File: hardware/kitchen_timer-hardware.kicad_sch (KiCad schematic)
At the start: 33 parts, among them J1 AVR-ISP-6, Q1 IRLML6402, SW1 SW_Push_Open_Dual, U1 ATmega328P-A, U2 BMS Module, U3 UART_Module, U4 AP2111H-3.3, U5 TPS61200DRC, Y1 Crystal

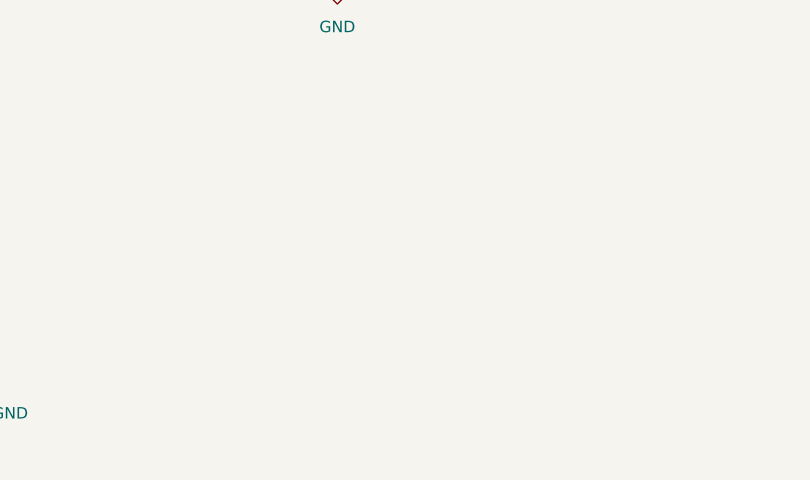
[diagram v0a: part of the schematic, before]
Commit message: Added the LED Matrices Driers as a hierarchical schematic.
I used the herachical schmatic feature cause it gives us more space to work on and organize connections.
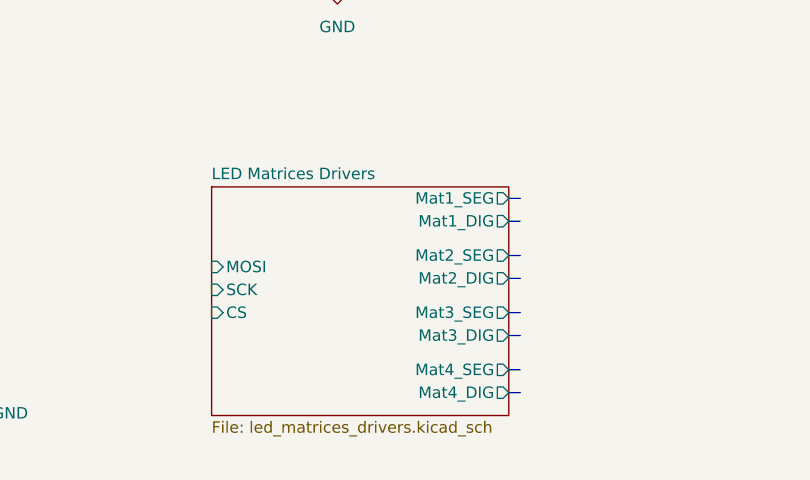
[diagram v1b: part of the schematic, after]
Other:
- added sheet LED Matrices Drivers (led_matrices_drivers.kicad_sch)
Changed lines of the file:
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@@
 		(at 109.22 30.48)
 	)
+	(bus
+		(pts
+			(xy 162.56 157.48) (xy 163.83 157.48)
+		)
+		(stroke
+			(width 0)
+			(type default)
+		)
+	)
 	(wire
 		(pts
@@
 		)
 	)
+	(bus
+		(pts
+			(xy 162.56 163.83) (xy 163.83 163.83)
+		)
+		(stroke
+			(width 0)
+			(type default)
+		)
+	)
 	(wire
 		(pts
@@
 		)
 	)
+	(bus
+		(pts
+			(xy 162.56 153.67) (xy 163.83 153.67)
+		)
+		(stroke
+			(width 0)
+			(type default)
+		)
+	)
+	(bus
+		(pts
+			(xy 162.56 151.13) (xy 163.83 151.13)
+		)
+		(stroke
+			(width 0)
+			(type default)
+		)
+	)
 	(wire
 		(pts
@@
 		)
 	)
+	(bus
+		(pts
+			(xy 162.56 160.02) (xy 163.83 160.02)
+		)
+		(stroke
+			(width 0)
+			(type default)
+		)
+	)
 	(wire
 		(pts
@@
 		)
 	)
+	(bus
+		(pts
+			(xy 162.56 170.18) (xy 163.83 170.18)
+		)
+		(stroke
+			(width 0)
+			(type default)
+		)
+	)
 	(wire
 		(pts
@@
 		)
 	)
+	(bus
+		(pts
+			(xy 162.56 166.37) (xy 163.83 166.37)
+		)
+		(stroke
+			(width 0)
+			(type default)
+		)
+	)
 	(wire
 		(pts
@@
 		)
 	)
+	(bus
+		(pts
+			(xy 162.56 172.72) (xy 163.83 172.72)
+		)
+		(stroke
+			(width 0)
+			(type default)
+		)
+	)
 	(wire
 		(pts
@@
 				)
 			)
+		)
+	)
+	(sheet
+		(at 129.54 149.86)
+		(size 33.02 25.4)
+		(fields_autoplaced yes)
+		(stroke
+			(width 0.1524)
+			(type solid)
+		)
+		(fill
+			(color 0 0 0 0.0000)
+		)
+		(property "Sheetname" "LED Matrices Drivers"
+			(at 129.54 149.1484 0)
+			(effects
+				(font
+					(size 1.27 1.27)
+				)
+				(justify left bottom)
+			)
+		)
+		(property "Sheetfile" "led_matrices_drivers.kicad_sch"
+			(at 129.54 175.8446 0)
+			(effects
+				(font
+					(size 1.27 1.27)
+				)
+				(justify left top)
+			)
+		)
+		(pin "MOSI" input
+			(at 129.54 158.75 180)
+			(effects
+				(font
+					(size 1.27 1.27)
+				)
+				(justify left)
+			)
+		)
+		(pin "SCK" input
+			(at 129.54 161.29 180)
+			(effects
+				(font
+					(size 1.27 1.27)
+				)
+				(justify left)
+			)
+		)
+		(pin "CS" input
+			(at 129.54 163.83 180)
+			(effects
+				(font
+					(size 1.27 1.27)
+				)
+				(justify left)
+			)
+		)
+		(pin "Mat2_DIG" output
+			(at 162.56 160.02 0)
+			(effects
+				(font
+					(size 1.27 1.27)
+				)
+				(justify right)
+			)
+		)
+		(pin "Mat2_SEG" output
+			(at 162.56 157.48 0)
+			(effects
+				(font
+					(size 1.27 1.27)
+				)
+				(justify right)
+			)
+		)
+		(pin "Mat1_SEG" output
+			(at 162.56 151.13 0)
+			(effects
+				(font
+					(size 1.27 1.27)
+				)
+				(justify right)
+			)
+		)
+		(pin "Mat1_DIG" output
+			(at 162.56 153.67 0)
+			(effects
+				(font
+					(size 1.27 1.27)
+				)
+				(justify right)
+			)
+		)
+		(pin "Mat3_SEG" output
+			(at 162.56 163.83 0)
+			(effects
+				(font
+					(size 1.27 1.27)
+				)
+				(justify right)
+			)
+		)
+		(pin "Mat3_DIG" output
+			(at 162.56 166.37 0)
+			(effects
+				(font
+					(size 1.27 1.27)
+				)
+				(justify right)
+			)
+		)
+		(pin "Mat4_DIG" output
+			(at 162.56 172.72 0)
+			(effects
+				(font
+					(size 1.27 1.27)
+				)
+				(justify right)
+			)
+		)
+		(pin "Mat4_SEG" output
+			(at 162.56 170.18 0)
+			(effects
+				(font
+					(size 1.27 1.27)
+				)
+				(justify right)
+			)
+		)
+		(instances
+			(project "kitchen_timer-hardware"
+				(path "/8963deea-96bc-4401-b671-98fbe9ed9c6a"
+					(page "2")
+				)
+			)

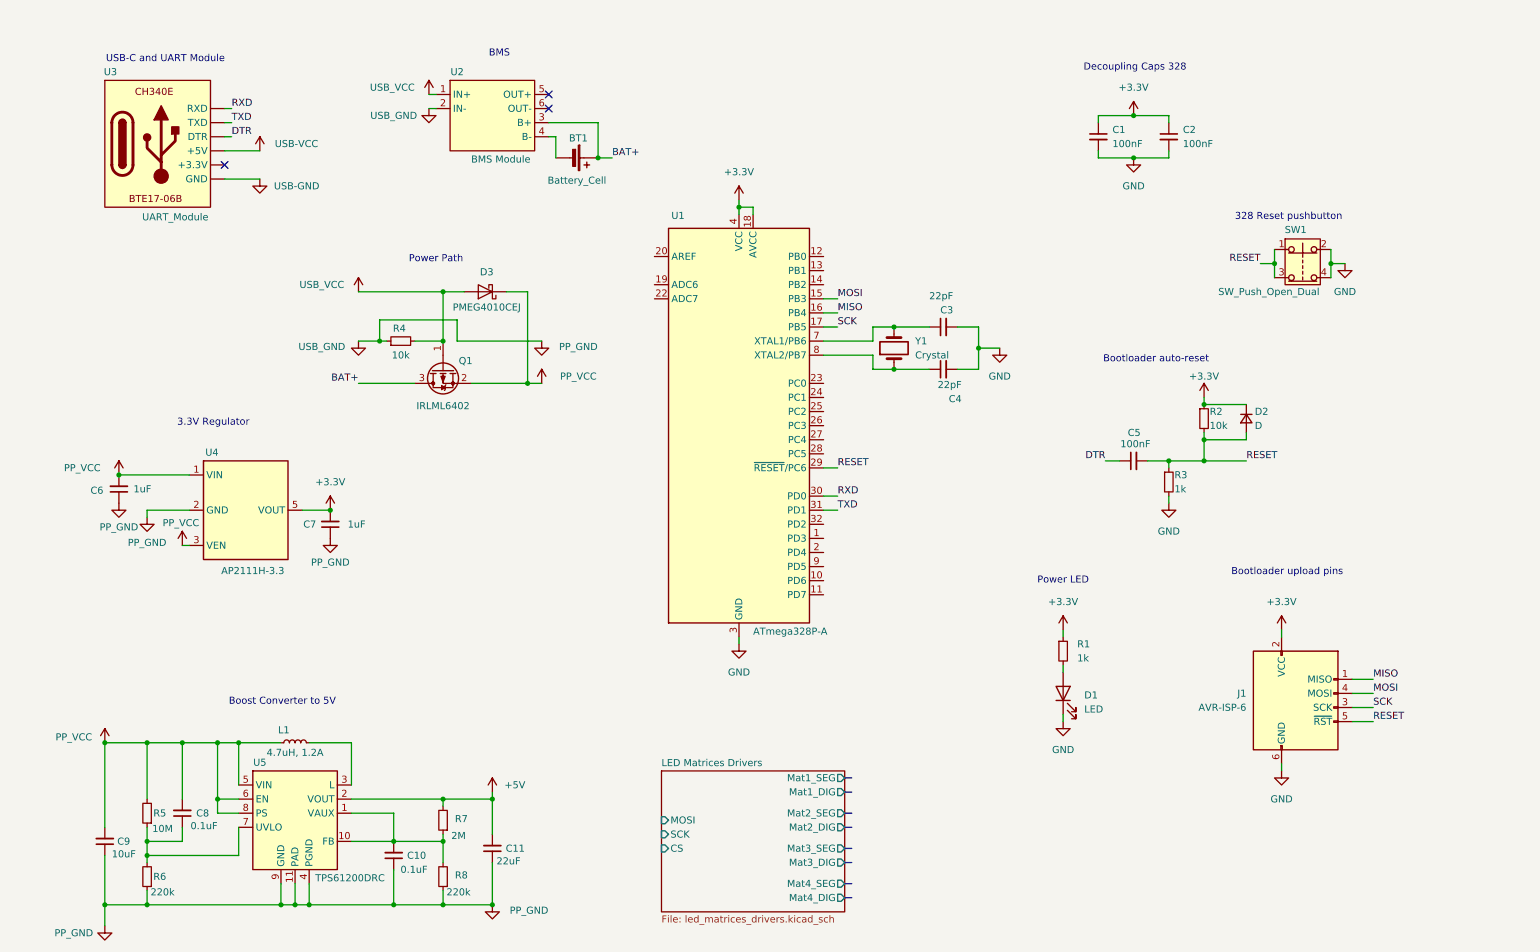
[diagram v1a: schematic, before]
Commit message: Added the LED Matrice Display schematic. Added LED Matrix symbol
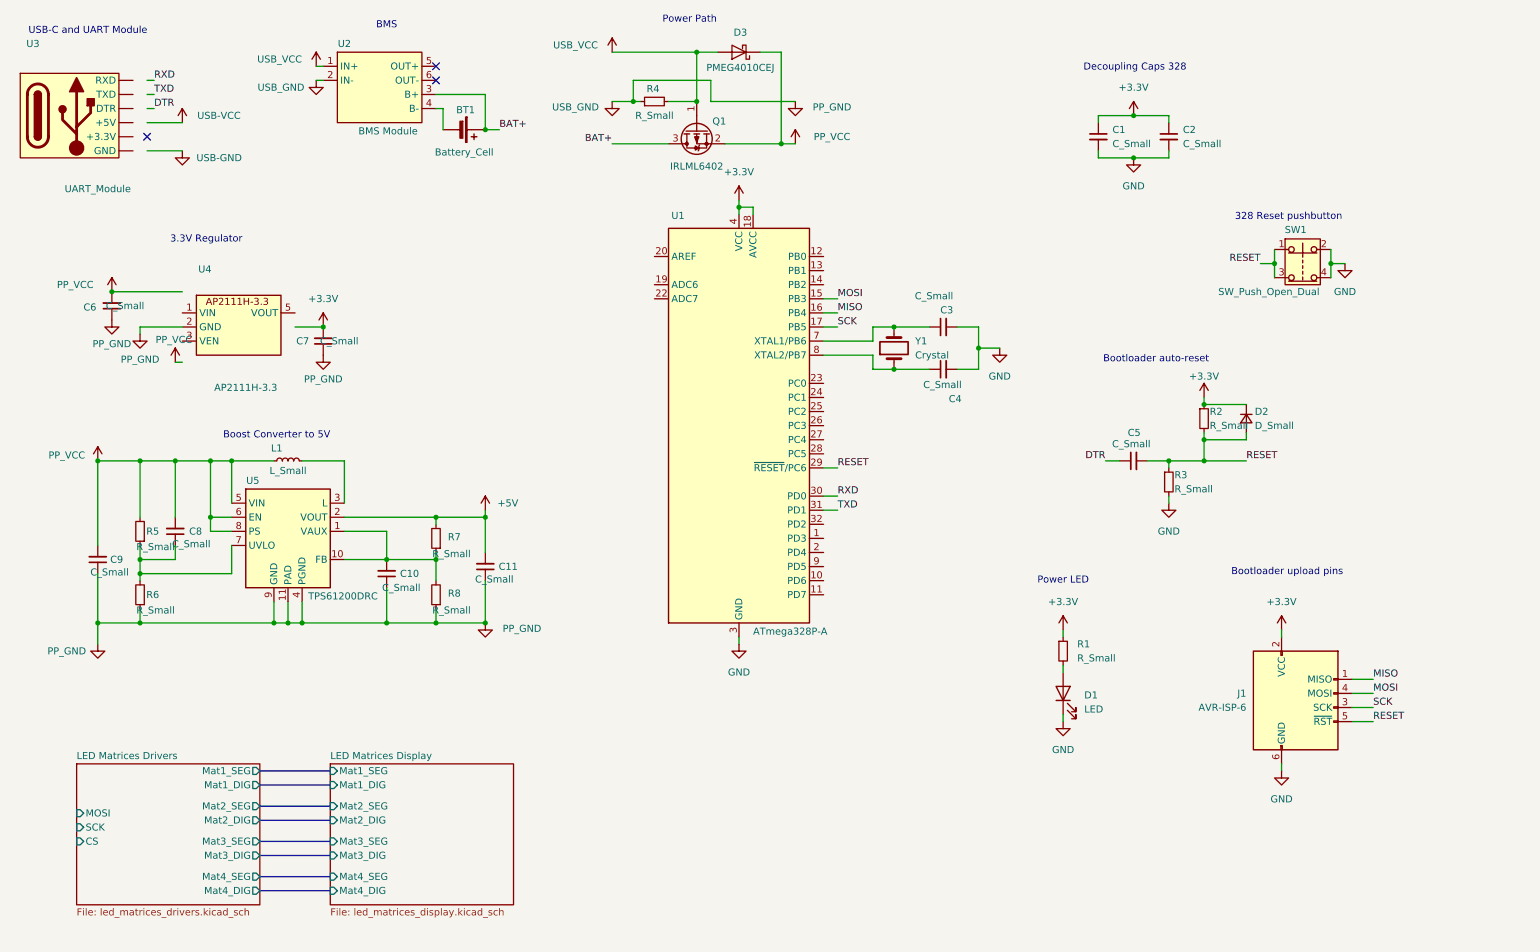
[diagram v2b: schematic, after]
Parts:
- C1, C2, C5: value 100nF -> C_Small
- C10, C8: value 0.1uF -> C_Small
- C11: value 22uF -> C_Small
- C3, C4: value 22pF -> C_Small
- C6, C7: value 1uF -> C_Small
- C9: value 10uF -> C_Small
- D2: value D -> D_Small
- L1: value 4.7uH, 1.2A -> L_Small
- R1, R3: value 1k -> R_Small
- R2, R4: value 10k -> R_Small
- R5: value 10M -> R_Small
- R6, R8: value 220k -> R_Small
- R7: value 2M -> R_Small
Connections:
- net +3.3V: no longer U4.5 (VOUT)
- net DTR: no longer U3. (TXD)
- net PP_VCC: no longer U4.1 (VIN), U4.3 (VEN)
- net RXD: no longer U3. (TXD)
- net TXD: no longer U3. (TXD)
- net USB-GND: no longer U3. (TXD)
- net USB-VCC: no longer U3. (TXD)
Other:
- added sheet LED Matrices Display (led_matrices_display.kicad_sch)
- title: Kitchen Timer -> Kitchen_Timer: Main
- moved on the sheet: BT1, C10, C11, C6, C7, C8, C9, D3, L1, Q1, R4, R5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

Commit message: Added the values of resostors and caps that for some reason got reseted.
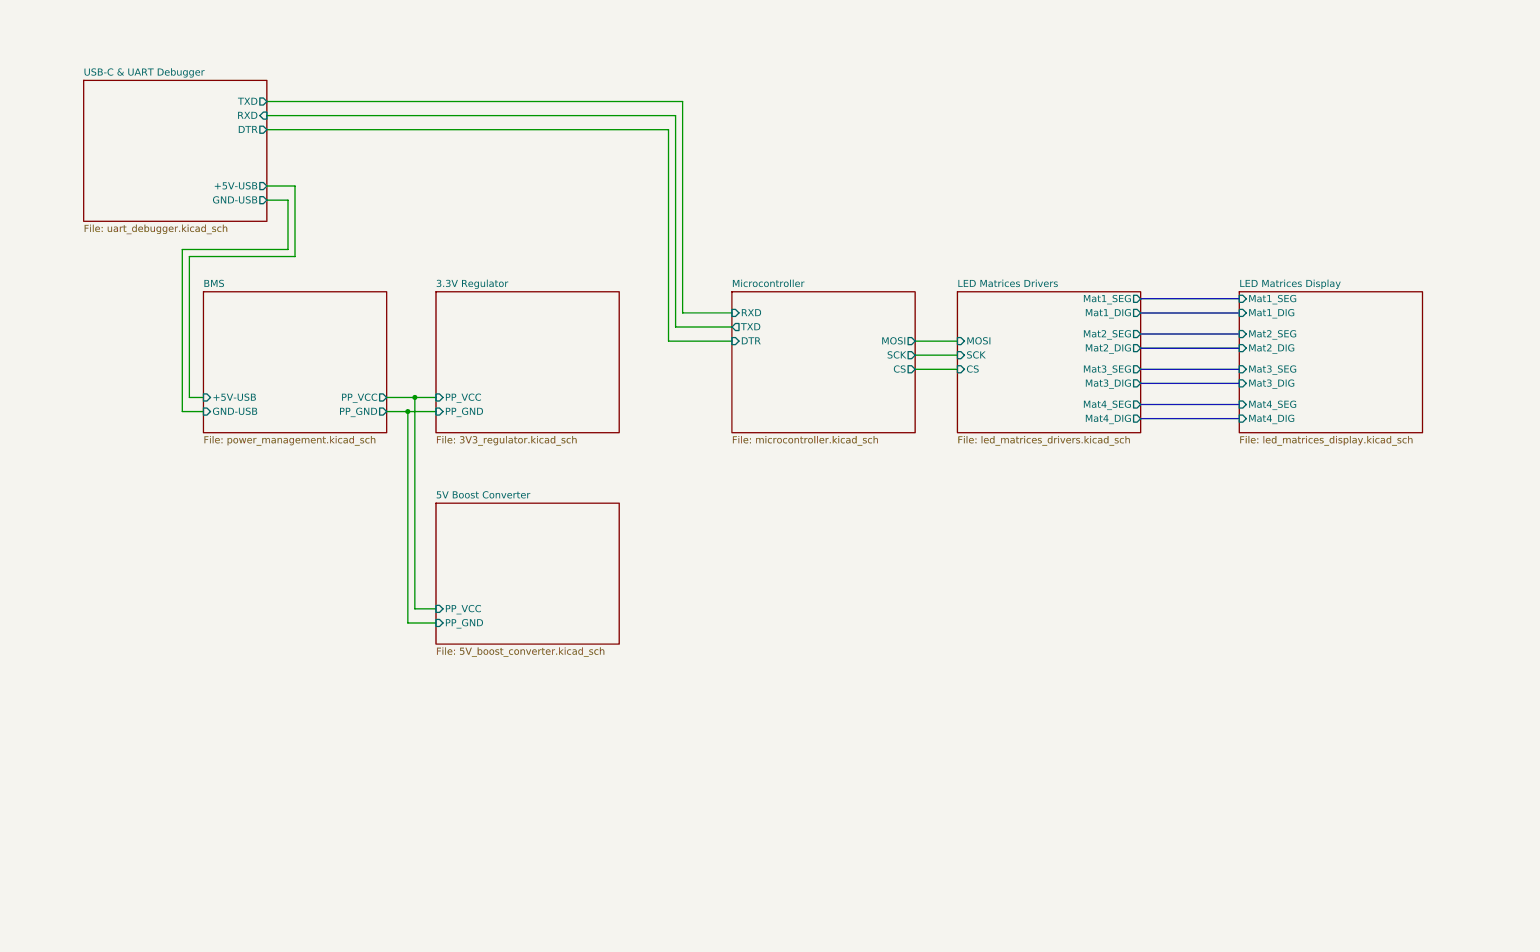
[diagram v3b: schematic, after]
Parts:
- removed BT1: Battery_Cell, symbol Device:Battery_Cell
- removed C1, C10, C11, C2, C3, C4, C5, C6, C7, C8, C9: C_Small, symbol Device:C_Small
- removed D1: LED, symbol Device:LED
- removed D2: D_Small, symbol Device:D_Small
- removed D3: PMEG4010CEJ, Diode_SMD:D_SOD-323F, symbol Diode:PMEG4010CEJ
- removed J1: AVR-ISP-6, symbol Connector:AVR-ISP-6
- removed L1: L_Small, symbol Device:L_Small
- removed Q1: IRLML6402, Package_TO_SOT_SMD:SOT-23, symbol Transistor_FET:IRLML6402
- removed R1, R2, R3, R4, R5, R6, R7, R8: R_Small, symbol Device:R_Small
- removed SW1: SW_Push_Open_Dual, symbol Switch:SW_Push_Open_Dual
- removed U1: ATmega328P-A, Package_QFP:TQFP-32_7x7mm_P0.8mm, symbol MCU_Microchip_ATmega:ATmega328P-A
- removed U2: BMS Module, symbol kitchen_timer-symbols_lib:BMS_Module
- removed U3: UART_Module, symbol kitchen_timer-symbols_lib:UART_Module
- removed U4: AP2111H-3.3, symbol kitchen_timer-symbols_lib:AP2111H-3.3TRG1
- removed U5: TPS61200DRC, Package_SON:Texas_S-PVSON-N10_ThermalVias, symbol Regulator_Switching:TPS61200DRC
- removed Y1: Crystal, symbol Device:Crystal
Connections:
- no-connect marks 3 -> 0
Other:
- added sheet 3.3V Regulator (3V3_regulator.kicad_sch)
- added sheet 5V Boost Converter (5V_boost_converter.kicad_sch)
- added sheet BMS (power_management.kicad_sch)
- added sheet Microcontroller (microcontroller.kicad_sch)
- added sheet USB-C & UART Debugger (uart_debugger.kicad_sch)
- note removed: "3.3V Regulator"
- note removed: "328 Reset pushbutton"
- note removed: "BMS"
- note removed: "Boost Converter to 5V"
- note removed: "Bootloader auto-reset"
- note removed: "Bootloader upload pins"
- note removed: "Decoupling Caps 328"
- note removed: "Power LED"
- note removed: "Power Path"
- note removed: "USB-C and UART Module"
- title: Kitchen_Timer: Main -> Kitchen_Timer - Main

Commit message: Added the piezo speaker circuit
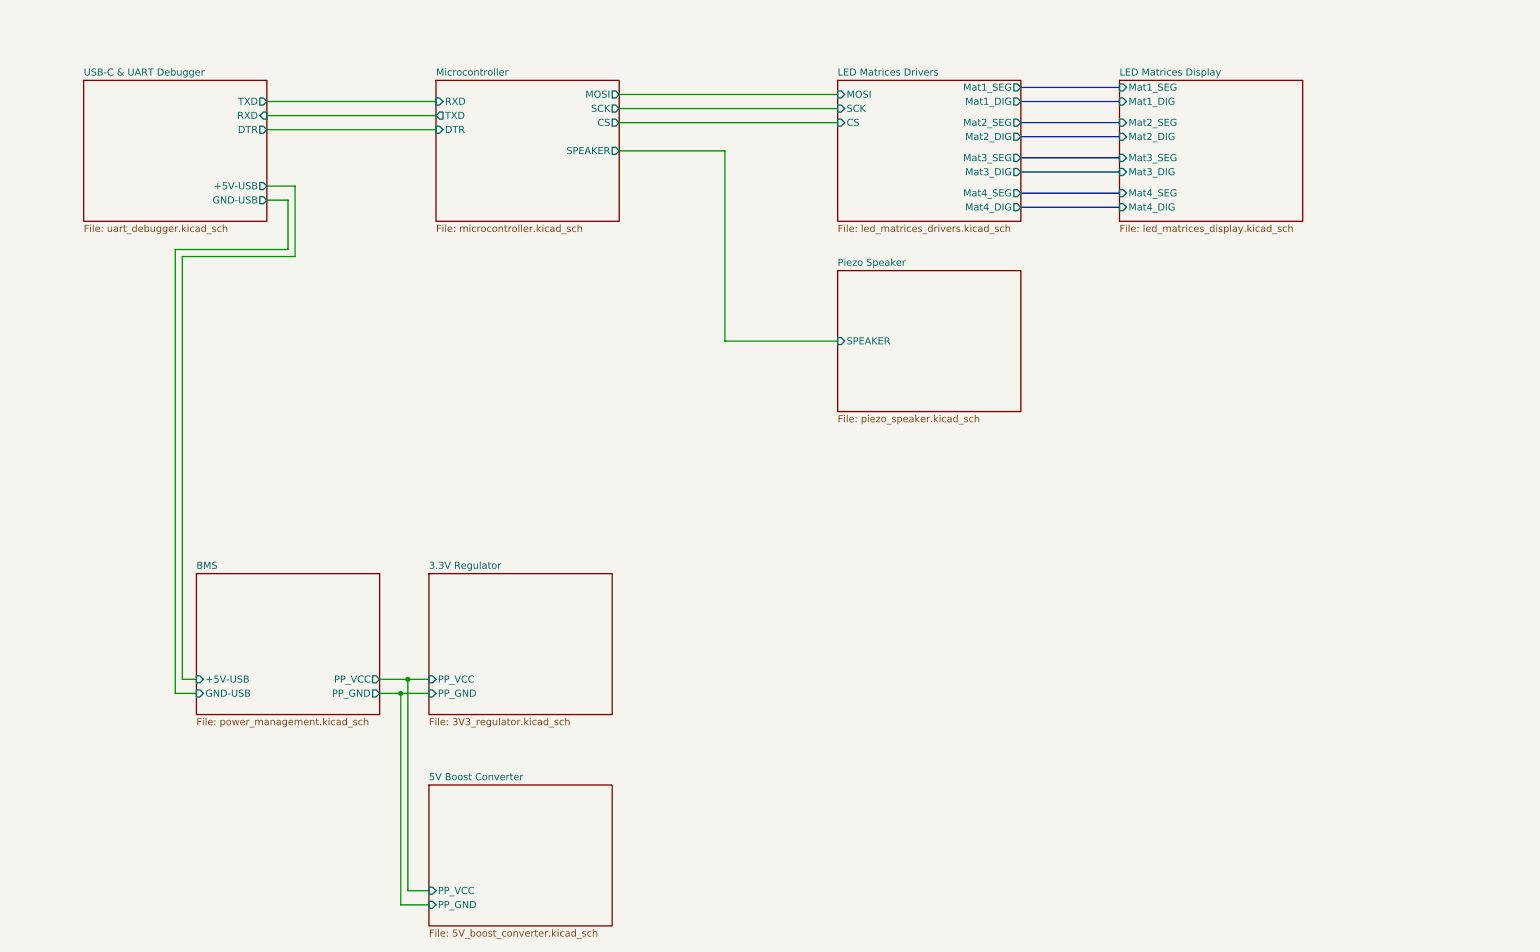
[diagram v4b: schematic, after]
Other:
- added sheet Piezo Speaker (piezo_speaker.kicad_sch)
- sheet Microcontroller ports: added SPEAKER; removed none
